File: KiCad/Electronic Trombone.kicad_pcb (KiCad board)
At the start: 2 copper layers, 150 x 130 mm, 173 parts, among them J1 691137710002, J2 691137710003, J3 691137710003, J4 691137710002, J5 691137710002, J6 691137710002, Q1 NPN, Q2 PNP, Q3 NPN, Q4 PNP, Q5 NPN, Q6 NPN, SW1 D6R90F2LFS, SW2 D6R90F2LFS, SW3 D6R90F2LFS, SW4 SW_DPST, U1 CD74HC4051E, U10 TL074, U11 TL074, U2 TL074, U3 TL074, U4 40106, U5 TL074, U6 TL074, U7 TL074, U8 TL074, U9 TL074

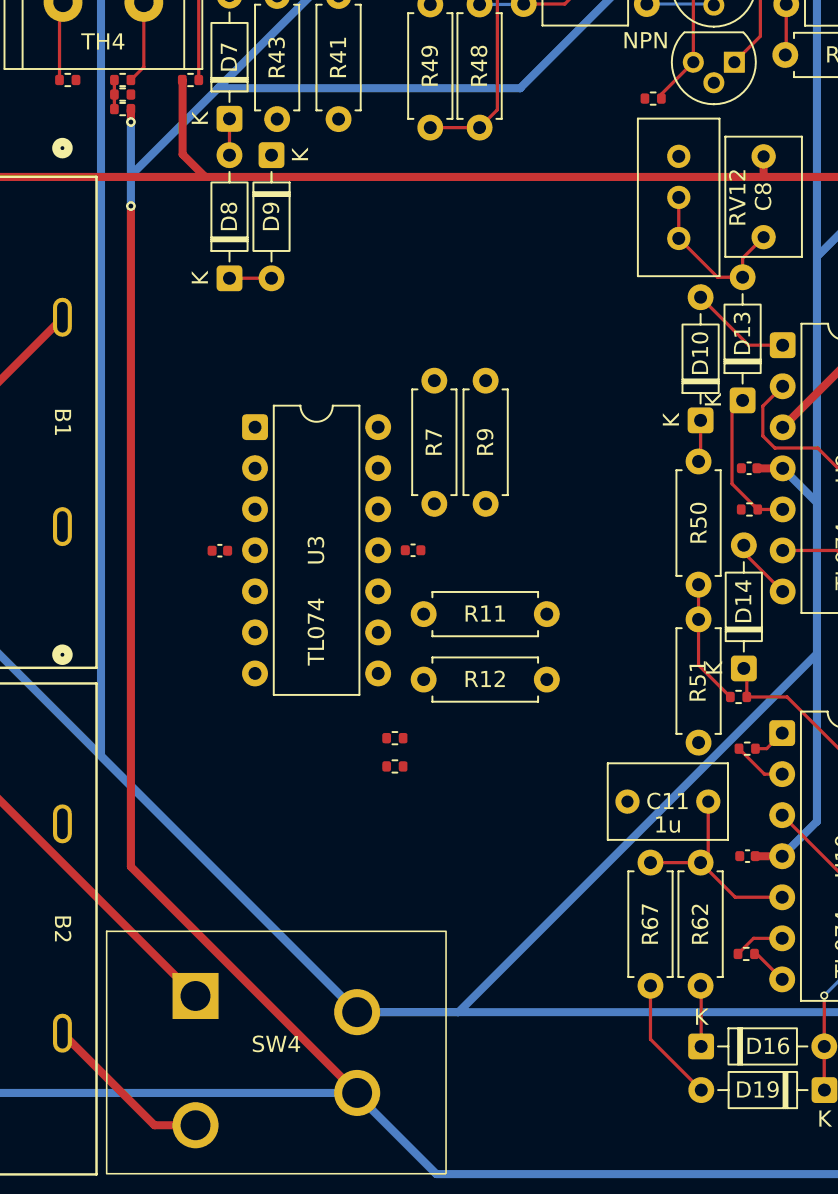
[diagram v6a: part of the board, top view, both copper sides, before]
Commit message: routed rest of the envelope generator
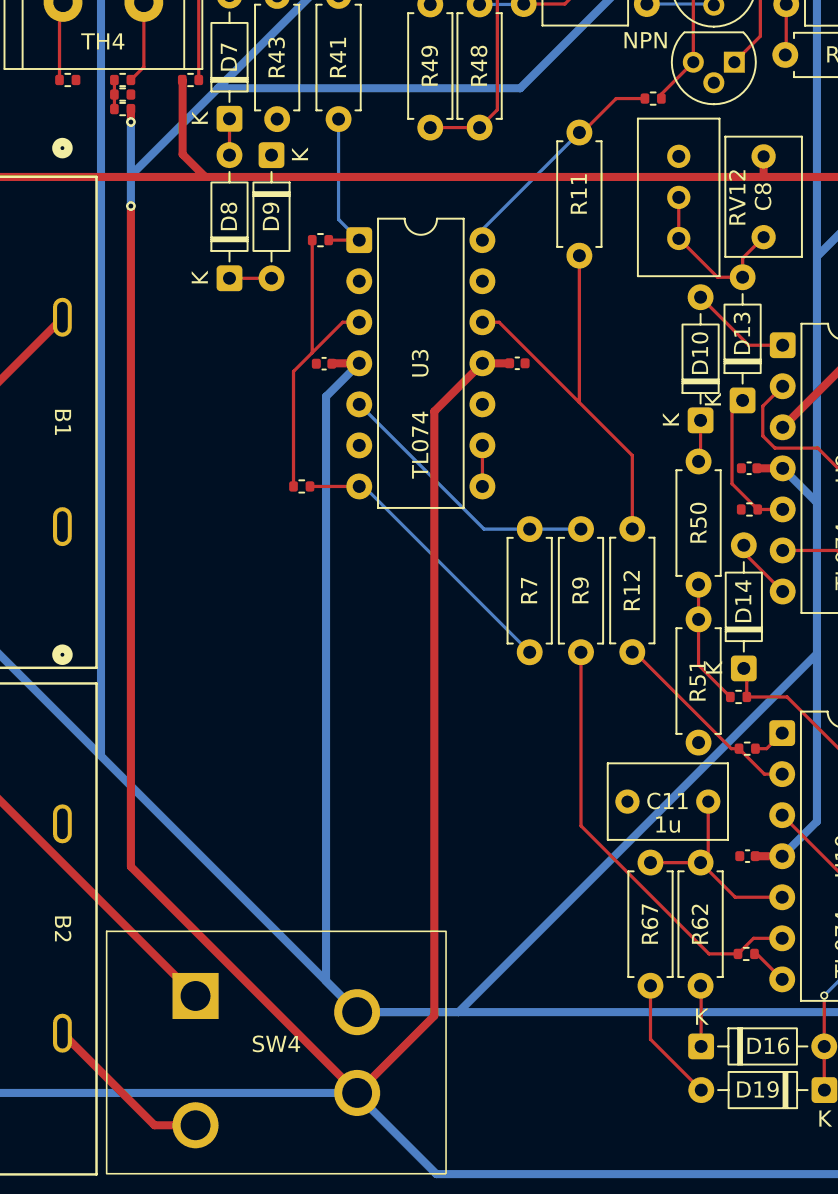
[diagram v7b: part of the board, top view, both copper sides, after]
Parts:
- moved R8 31.2 mm to (119.6, 93.4)
- moved R11 24.2 mm to (135.7, 94.4), turned to 90 degrees
- moved R10 18.3 mm to (118.5, 108.7), turned to 180 degrees
- moved U3 13.2 mm to (122.0, 93.4)
- moved C14 13.2 mm to (119.9, 101.1)
- moved C15 13.2 mm to (131.8, 101.0)
- moved R12 13.0 mm to (138.9, 118.9), turned to 90 degrees
- moved R9 10.9 mm to (135.8, 118.9)
- moved R7 10.9 mm to (132.6, 111.3)
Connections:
- R7 pad 1: Net-(U3C-+) -> Net-(U3B-+)
- R9 pad 2: Net-(U3C-+) -> Net-(U3B-+)
- U3 pad 10: Net-(U3C-+) -> GND
- U3 pad 5: GND -> Net-(U3B-+)
- U3 pad 6: /Power/Thaw 3 -> GND
- U3 pad 7: /Power/Thaw 3 -> Net-(R10-Pad1)
- U3 pad 8: Net-(R10-Pad1) -> /Power/Thaw 3
- U3 pad 9: GND -> /Power/Thaw 3
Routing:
- net -9V: track 454.7 -> 504.7 mm
- net Net-(U3D-+): track 0.00 -> 26.3 mm
- net //Envelope Generator/Out Filter: track 3.13 -> 26.9 mm
- net +9V: track 474.4 -> 495.4 mm
- net Net-(U3A-+): track 0.00 -> 19.4 mm
- net Net-(R10-Pad1): track 0.00 -> 17.8 mm
- net Net-(U3B-+): track 0.00 -> 16.9 mm
- net //Amp Control: track 0.00 -> 14.1 mm
- net //Filter Control: track 0.00 -> 9.91 mm
- net //Envelope Generator/Out Amp: track 3.33 -> 12.4 mm
- net /Power/Thaw 3: track 0.00 -> 2.54 mm

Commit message: checkpoint before attempt to reroute power traces
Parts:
- moved R72 11.7 mm to (172.6, 138.9), turned to 180 degrees
- moved C7 3.85 mm to (193.4, 60.5)
- moved RV14 2.58 mm to (187.7, 143.7), turned to -90 degrees
- moved R26 1.71 mm to (128.5, 58.3)
- moved R16 1.64 mm to (63.6, 58.9), turned to 180 degrees
- moved R17 1.39 mm to (53.4, 58.1)
- moved TH2 1.39 mm to (53.7, 62.9)
- moved Q1 1.39 mm to (65.4, 63.5)
- moved Q2 1.39 mm to (64.6, 66.5)
- moved R13 1.39 mm to (55.1, 85.8)
- moved R14 1.39 mm to (55.1, 84.7)
- moved R15 1.39 mm to (55.1, 86.9)
- moved R18 1.39 mm to (51.3, 84.8)
- moved R19 1.39 mm to (59.2, 84.8)
- moved TH1 1.39 mm to (53.7, 79.9)
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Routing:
- net +9V: track 495.4 -> 321.4 mm, vias 2 -> 1
- net //Oscillator/Core In 2: track 4.89 -> 28.0 mm
- net +5V: track 199.7 -> 210.7 mm
- net Net-(U11D-+): track 3.50 -> 11.8 mm
- net -9V: track 504.7 -> 512.9 mm, vias 7 -> 8
- net Net-(Q1-B): track 7.64 -> 0.00 mm
- net Net-(D5-K): track 16.9 -> 21.0 mm
- net //Oscillator/Mix In 2: track 48.6 -> 45.0 mm
- net Net-(U7A-+): track 14.0 -> 16.2 mm
- net //Oscillator/Core In 1: track 28.5 -> 30.6 mm
- net Net-(R5-Pad2): track 43.7 -> 42.3 mm
- net Net-(U2D-+): track 19.8 -> 18.5 mm
- net Net-(C2-Pad1): track 10.4 -> 11.4 mm
- net //Oscillator/Sch Inv Out 2: track 14.3 -> 13.2 mm
- net //Oscillator/Sch Inv In 1: track 38.1 -> 37.3 mm
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- added copper zone on B.Cu, net GND
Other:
- board text removed: "Adj Cust Pot Diff"
